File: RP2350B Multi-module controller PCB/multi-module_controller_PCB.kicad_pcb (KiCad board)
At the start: 4 copper layers, 59.8 x 85 mm, 71 parts, among them J4 SM03B-SRSS-TB, SW1 SW_Push, SW10 BTN_MDL, SW2 SW_Push, SW3 BTN_LEFT, SW4 BTN_UP, SW5 BTN_OK, SW6 BTN_DOWN, SW7 BTN_RIGHT, SW8 BTN_BACK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

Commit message: all core components placed and routed
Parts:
- added J5: USB_C_Receptacle_USB2.0_14P, Connector_USB:USB_C_Receptacle_G-Switch_GT-USB-7010ASV, F.Cu at (100.1, 71.8)
- added J6: USB_C_Receptacle_USB2.0_14P, Connector_USB:USB_C_Receptacle_G-Switch_GT-USB-7010ASV, F.Cu at (62.9, 87.0)
- added J7: Module_Bay, Connector_PinHeader_2.54mm:PinHeader_1x08_P2.54mm_Vertical, F.Cu at (60.7, 135.7)
- added J8: USB_A, Connector_USB:USB_A_Connfly_DS1095, F.Cu at (72.0, 97.3)
- moved R20 74.1 mm to (64.8, 135.1), turned to 90 degrees
- moved R21 65.9 mm to (65.1, 127.9)
- moved C19 65.0 mm to (91.9, 109.1), turned to 90 degrees
- moved R22 61.9 mm to (65.0, 125.5)
- moved R5 60.2 mm to (93.3, 73.5), turned to 180 degrees
- moved R12 59.9 mm to (93.3, 72.3), turned to 180 degrees
- moved C24 58.7 mm to (65.4, 131.4), turned to -90 degrees
- moved C25 52.2 mm to (63.3, 131.7), turned to -90 degrees
- moved R17 49.9 mm to (79.0, 93.0), turned to 90 degrees
- moved R14 49.7 mm to (77.9, 93.0), turned to 90 degrees
- moved R19 46.2 mm to (79.2, 82.8), turned to -90 degrees
- moved R18 45.3 mm to (78.0, 82.8), turned to -90 degrees
- moved C23 37.6 mm to (93.5, 77.0), turned to 180 degrees
- moved R23 28.5 mm to (63.9, 80.2), turned to 180 degrees
- moved R24 27.7 mm to (63.9, 78.4), turned to 180 degrees
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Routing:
- net VBUS: track 12.1 -> 122.9 mm, vias 0 -> 4
- net GND: track 33.9 -> 126.7 mm, vias 28 -> 46
- net /GPIO13: track 8.02 -> 55.8 mm, vias 0 -> 2
- net /GPIO12: track 10.2 -> 52.5 mm, vias 0 -> 2
- net /GPIO24: track 6.66 -> 42.8 mm
- net /GPIO16: track 6.29 -> 40.3 mm, vias 0 -> 2
- net +3V3: track 52.9 -> 83.0 mm, vias 3 -> 18
- net /GPIO11: track 2.07 -> 31.1 mm, vias 0 -> 2
- net Net-(U6-OUTA): track 0.00 -> 27.3 mm, vias 0 -> 3
- net /GPIO10: track 1.97 -> 27.9 mm
- net /GPIO22: track 3.59 -> 26.3 mm, vias 0 -> 2
- net /GPIO9: track 1.86 -> 23.7 mm
- net /GPIO23: track 3.41 -> 23.2 mm, vias 0 -> 2
- net Net-(U5-HSD1+): track 0.00 -> 18.2 mm
- net /GPIO7: track 1.00 -> 19.2 mm, vias 0 -> 2
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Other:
- board size 59.8 x 85 mm -> 59.8 x 84.4 mm
- board text added: "2.5, 2.9"

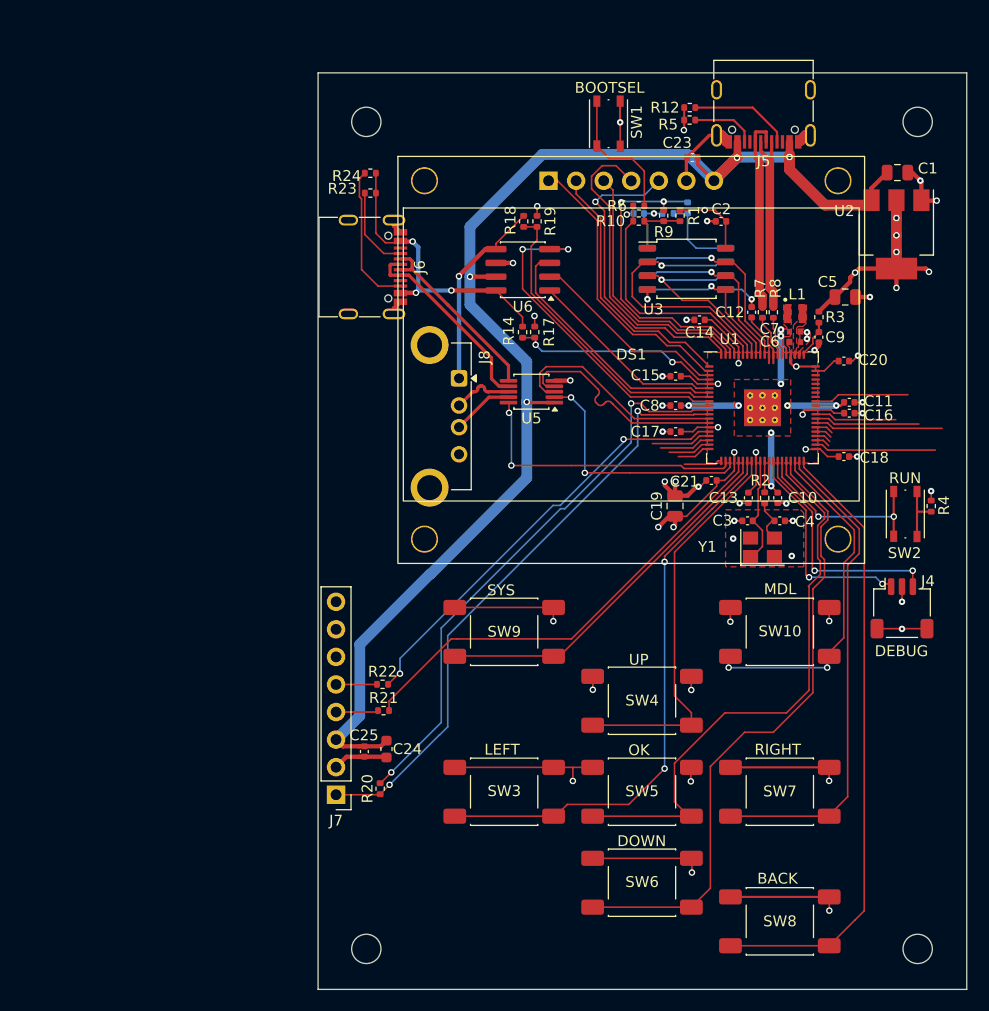
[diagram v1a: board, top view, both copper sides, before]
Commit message: minor tweaks to USB port overhang positioning
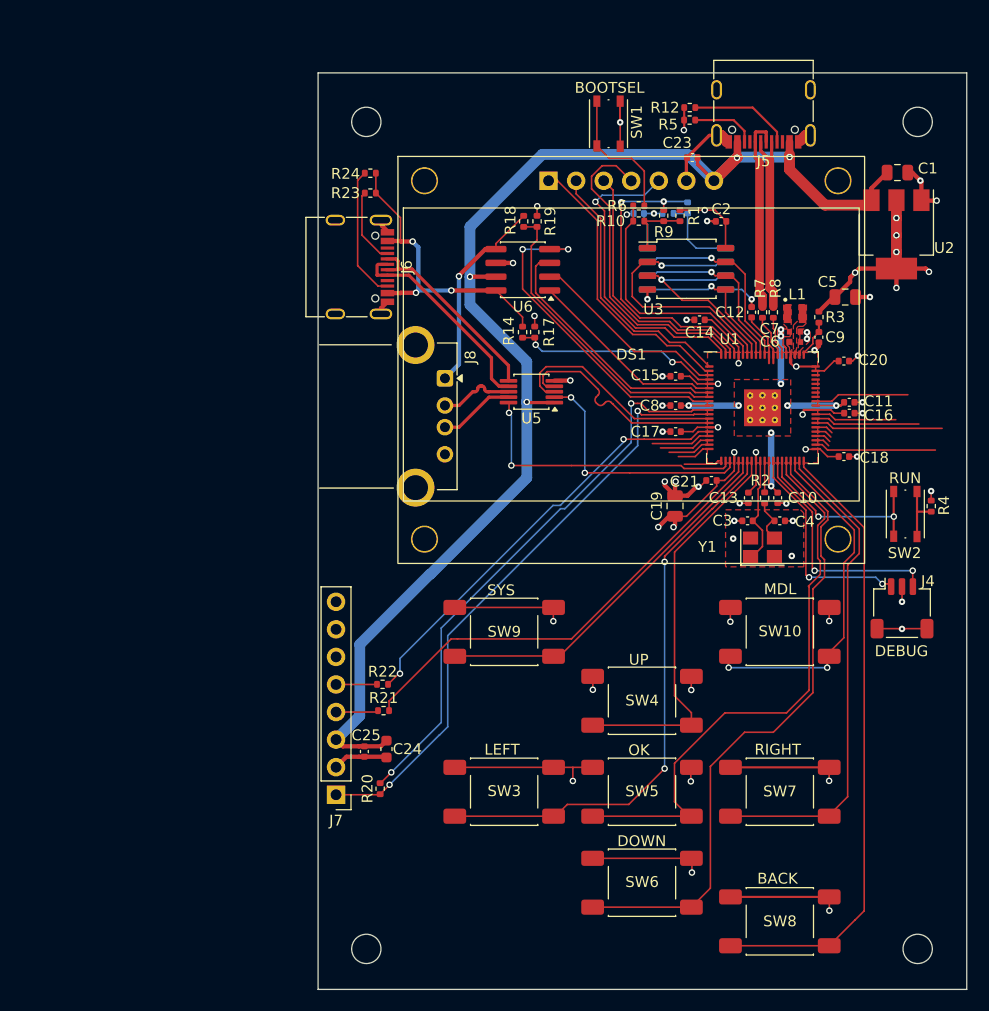
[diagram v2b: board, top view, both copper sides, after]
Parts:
- moved J8 1.30 mm to (70.7, 97.3)
- moved J6 1.20 mm to (61.7, 87.0)
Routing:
- net Net-(U6-OUTA): track 27.3 -> 28.7 mm
- net Net-(J8-D-): track 5.66 -> 6.96 mm
- net Net-(J8-D+): track 5.70 -> 7.00 mm
- net Net-(U5-HSD1-): track 17.0 -> 18.1 mm
- net Net-(U5-HSD1+): track 18.2 -> 19.3 mm
- net Net-(J6-CC2): track 13.4 -> 12.3 mm
- net Net-(J8-VBUS): track 17.6 -> 18.6 mm
- net Net-(J6-CC1): track 7.82 -> 7.03 mm
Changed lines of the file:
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@@
 		(tags "CMS SOT")
 		(property "Reference" "U2"
-			(at -2.15 4.8 0)
+			(at 1.25 -4.4 0)
 			(layer "F.SilkS")
 			(effects
@@
 	(footprint "Connector_USB:USB_A_Connfly_DS1095"
 		(layer "F.Cu")
-		(at 72.0428 97.2918 -90)
+		(at 70.7428 97.2918 -90)
 		(descr "USB type A receptacle, THT, horizontal, https://en.connfly.com/static/upload/file/DS1095.pdf")
 		(tags "Connfly female socket through-hole")
@@
 		(tags "capacitor")
 		(property "Reference" "C25"
-			(at -1.5 0.04 180)
+			(at -1.5 -0.16 180)
 			(layer "F.SilkS")
 			(effects
@@
 		(tags "resistor")
 		(property "Reference" "R24"
-			(at 2.1844 -0.2556 0)
+			(at 2.2844 -0.0556 0)
 			(layer "F.SilkS")
 			(effects
@@
 	(footprint "Connector_USB:USB_C_Receptacle_G-Switch_GT-USB-7010ASV"
 		(layer "F.Cu")
-		(at 62.9214 87.0366 -90)
+		(at 61.7214 87.0366 -90)
 		(descr "USB Type C, right-angle, SMT, https://datasheet.lcsc.com/lcsc/2204071530_G-Switch-GT-USB-7010ASV_C2988369.pdf")
 		(tags "USB C Type-C Receptacle SMD")
@@
 		(tags "resistor")
 		(property "Reference" "R23"
-			(at 2.5908 0.4048 0)
+			(at 2.2908 0.0048 0)
 			(layer "F.SilkS")
 			(effects
@@
 		)
 	)
+	(gr_line
+		(start 66 107.4)
+		(end 59.2 107.4)
+		(stroke
+			(width 0.12)
+			(type default)
+		)
+		(layer "F.SilkS")
+	)
+	(gr_line
+		(start 65.8 94.2)
+		(end 59.2 94.2)
+		(stroke
+			(width 0.12)
+			(type default)
+		)
+		(layer "F.SilkS")
+	)
 	(gr_rect
 		(start 59.055 69.145)
@@
 	)
 	(segment
-		(start 66.0464 91.3566)
-		(end 66.0464 90.8366)
+		(start 64.8464 91.3566)
+		(end 64.8464 90.8366)
 		(width 0.4)
 		(layer "F.Cu")
@@
 	)
 	(segment
-		(start 66.0464 83.2366)
-		(end 66.6464 83.8366)
+		(start 64.9464 83.2366)
+		(end 65.5464 83.8366)
 		(width 0.4)
 		(layer "F.Cu")
@@
 	)
 	(segment
-		(start 66.0464 90.8366)
-		(end 66.6464 90.2366)
+		(start 64.8464 90.8366)
+		(end 65.4464 90.2366)
 		(width 0.4)
 		(layer "F.Cu")
@@
 	)
 	(segment
-		(start 66.0464 82.7166)
-		(end 66.0464 83.2366)
+		(start 64.9464 82.7166)
+		(end 64.9464 83.2366)
 		(width 0.4)
 		(layer "F.Cu")
@@
 	)
 	(segment
-		(start 76.5983 97.524)
-		(end 76.5983 96.1055)
+		(start 66.4164 86.4846)
+		(end 66.2184 86.2866)
 		(width 0.3)
 		(layer "F.Cu")
@@
 	)
 	(segment
-		(start 76.5983 96.1055)
-		(end 71.0184 90.5256)
+		(start 66.4164 87.1728)
+		(end 66.4164 86.4846)
 		(width 0.3)
 		(layer "F.Cu")
@@
 	)
 	(segment
-		(start 67.7164 87.1728)
-		(end 67.6026 87.2866)
-		(width 0.3)
-		(layer "F.Cu")
-		(net 75)
-	)
-	(segment
-		(start 67.7164 87.2236)
-		(end 67.7164 87.1728)
+		(start 76.5983 96.1055)
+		(end 67.7164 87.2236)
 		(width 0.3)
 		(layer "F.Cu")
@@
 	)
 	(segment
-		(start 67.7164 87.1728)
-		(end 67.7164 86.4846)
+		(start 66.4672 87.2236)
+		(end 66.4164 87.1728)
 		(width 0.3)
 		(layer "F.Cu")
@@
 	)
 	(segment
-		(start 67.5184 86.2866)
-		(end 66.6464 86.2866)
+		(start 66.2184 86.2866)
+		(end 65.3464 86.2866)
 		(width 0.3)
 		(layer "F.Cu")
@@
 	)
 	(segment
-		(start 71.0184 90.5256)
-		(end 67.7164 87.2236)
+		(start 66.3026 87.2866)
+		(end 65.3464 87.2866)
 		(width 0.3)
 		(layer "F.Cu")
@@
 	)
 	(segment
-		(start 67.6026 87.2866)
-		(end 66.6464 87.2866)
+		(start 67.7164 87.2236)
+		(end 66.4672 87.2236)
 		(width 0.3)
 		(layer "F.Cu")
@@
 	)
 	(segment
-		(start 67.7164 86.4846)
-		(end 67.5184 86.2866)
+		(start 76.5983 97.524)
+		(end 76.5983 96.1055)
 		(width 0.3)
 		(layer "F.Cu")
@@
 	)
 	(segment
-		(start 74.8106 99.024)
-		(end 72.0428 101.7918)
+		(start 76.5983 99.024)
+		(end 74.8106 99.024)
 		(width 0.3)
 		(layer "F.Cu")
@@
 	)
 	(segment
-		(start 76.5983 99.024)
-		(end 74.8106 99.024)
+		(start 72.0428 101.7918)
+		(end 70.7428 101.7918)
 		(width 0.3)
 		(layer "F.Cu")
@@
 	)
 	(segment
-		(start 76.5983 98.024)
-		(end 75.733952 98.024)
+		(start 74.8106 99.024)
+		(end 72.0428 101.7918)
 		(width 0.3)
 		(layer "F.Cu")
-		(net 77)
+		(net 76)
 	)
 	(segment
-		(start 75.733952 98.024)
-		(end 75.0316 97.321648)
+		(start 67.4158 87.7866)
+		(end 65.4464 87.7866)
 		(width 0.3)
 		(layer "F.Cu")
@@
 	)
 	(segment
-		(start 65.6886 86.8724)
-		(end 65.7744 86.7866)
+		(start 64.5744 86.7866)
+		(end 65.4464 86.7866)
 		(width 0.3)
 		(layer "F.Cu")
@@
 	)
 	(segment
-		(start 65.7744 86.7866)
-		(end 66.6464 86.7866)
+		(start 65.4464 87.7866)
+		(end 64.4886 87.7866)
 		(width 0.3)
 		(layer "F.Cu")
@@
 	)
 	(segment
-		(start 66.6464 87.7866)
-		(end 65.6886 87.7866)
+		(start 75.733952 98.024)
+		(end 75.0316 97.321648)
 		(width 0.3)
 		(layer "F.Cu")
@@
 	)
 	(segment
-		(start 67.4158 87.7866)
-		(end 66.6464 87.7866)
+		(start 76.5983 98.024)
+		(end 75.733952 98.024)
 		(width 0.3)
 		(layer "F.Cu")
@@
 	)
 	(segment
-		(start 65.6886 87.7866)
-		(end 65.6886 86.8724)
+		(start 64.4886 87.7866)
+		(end 64.4886 86.8724)
 		(width 0.3)
 		(layer "F.Cu")
@@
 	)
 	(segment
+		(start 72.0428 99.7918)
+		(end 70.7428 99.7918)
+		(width 0.3)
+		(layer "F.Cu")
+		(net 78)
+	)
+	(segment
 		(start 73.75661 98.268)
 		(end 73.75661 98.25)
@@
 	)
 	(segment
-		(start 72.0428 87.8924)
-		(end 72.0344 87.884)
+		(start 72.0344 96.0002)
+		(end 70.7428 97.2918)
 		(width 0.4)
 		(layer "B.Cu")
@@
 	)
 	(segment
-		(start 72.0428 96.8918)
-		(end 72.0428 87.8924)
+		(start 72.0344 87.884)
+		(end 72.0344 96.0002)
+		(width 0.4)
+		(layer "B.Cu")
+		(net 79)
+	)
+	(segment
+		(start 72.0428 87.8924)
+		(end 72.0344 87.884)
 		(width 0.4)
 		(layer "B.Cu")
@@
 	(segment
 		(start 66.6464 84.6366)
-		(end 66.4854 84.7976)
-		(width 0.15)
+		(end 65.4464 84.6366)
+		(width 0.4)
 		(layer "F.Cu")
 		(net 80)
 	)
 	(segment
-		(start 77.8968 92.525)
-		(end 77.8968 91.6488)
-		(width 0.15)
+		(start 66.6934 84.6836)
+		(end 66.6464 84.6366)
+		(width 0.4)
 		(layer "F.Cu")
 		(net 80)
 	)
 	(segment
-		(start 66.4854 84.7976)
-		(end 65.256747 84.7976)
+		(start 66.675 89.408)
+		(end 66.6464 89.4366)
+		(width 0.4)
+		(layer "F.Cu")
+		(net 80)
+	)
+	(segment
+		(start 77.8968 92.525)
+		(end 77.8968 91.6488)
 		(width 0.15)
 		(layer "F.Cu")
@@
 	)
 	(segment
-		(start 66.6934 84.6836)
-		(end 66.6464 84.6366)
-		(width 0.4)
-		(layer "F.Cu")
-		(net 80)
-	)
-	(segment
-		(start 64.3816 83.922453)
-		(end 64.3816 80.2222)
+		(start 64.3816 80.2222)
+		(end 64.3816 80.1184)
 		(width 0.15)
 		(layer "F.Cu")
@@
 	)
 	(segment
-		(start 64.3816 80.2222)
-		(end 64.3816 80.1184)
+		(start 66.6464 82.487)
+		(end 66.6464 84.6366)
 		(width 0.15)
 		(layer "F.Cu")
@@
 	)
 	(segment
-		(start 66.675 89.408)
-		(end 66.6464 89.4366)
+		(start 66.6464 89.4366)
+		(end 65.4464 89.4366)
 		(width 0.4)
 		(layer "F.Cu")
@@
 	)
 	(segment
-		(start 65.256747 84.7976)
-		(end 64.3816 83.922453)
+		(start 64.38 80.1168)
+		(end 64.38 78.3878)
 		(width 0.15)
 		(layer "F.Cu")
@@
 	)
 	(segment
-		(start 64.38 80.1168)
-		(end 64.38 78.3878)
+		(start 64.3816 80.2222)
+		(end 66.6464 82.487)
 		(width 0.15)
 		(layer "F.Cu")
@@
 	)
 	(segment
-		(start 66.6464 85.7866)
-		(end 65.111 85.7866)
+		(start 63.1 84.1)
+		(end 64.7866 85.7866)
 		(width 0.15)
 		(layer "F.Cu")
@@
 	)
 	(segment
-		(start 65.111 85.7866)
-		(end 63.3616 84.0372)
+		(start 63.1 80.4838)
+		(end 63.1 84.1)
 		(width 0.15)
 		(layer "F.Cu")
@@
 	)
 	(segment
-		(start 63.3616 84.0372)
-		(end 63.3616 80.2222)
+		(start 64.7866 85.7866)
+		(end 65.4464 85.7866)
 		(width 0.15)
 		(layer "F.Cu")
@@
 	)
 	(segment
-		(start 63.0606 80.755474)
-		(end 63.0606 87.2686)
+		(start 63.3616 80.2222)
+		(end 63.1 80.4838)
 		(width 0.15)
 		(layer "F.Cu")
-		(net 86)
+		(net 85)
 	)
 	(segment
-		(start 64.5786 88.7866)
-		(end 66.6464 88.7866)
+		(start 62.7 79.0478)
+		(end 63.36 78.3878)
 		(width 0.15)
 		(layer "F.Cu")
@@
 	)
 	(segment
-		(start 63.36 78.3878)
-		(end 62.8656 78.8822)
+		(start 64.5786 88.7866)
+		(end 62.7 86.908)
 		(width 0.15)
 		(layer "F.Cu")
@@
 	)
 	(segment
-		(start 62.8656 80.560474)
-		(end 63.0606 80.755474)
+		(start 62.7 86.908)
+		(end 62.7 79.0478)
 		(width 0.15)
 		(layer "F.Cu")
@@
 	)
 	(segment
-		(start 63.0606 87.2686)
+		(start 65.4464 88.7866)
 		(end 64.5786 88.7866)
 		(width 0.15)
 		(layer "F.Cu")
-		(net 86)
-	)
-	(segment
-		(start 62.8656 78.8822)
-		(end 62.8656 80.560474)
-		(width 0.15)
-		(layer "F.Cu")

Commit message: completed layout, include production files, before adjusting component mounting
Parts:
- added J1: Conn_02x06_Odd_Even, Connector_PinSocket_2.54mm:PinSocket_2x06_P2.54mm_Vertical, F.Cu at (68.8, 71.6)
- added J9: ADC_Breakout, Connector_JST:JST_PH_B12B-PH-K_1x12_P2.00mm_Vertical, F.Cu at (116.3, 91.2)
- added R15: 10k, Resistor_SMD:R_0402_1005Metric, F.Cu at (83.3, 86.5)
- added R16: 10k, Resistor_SMD:R_0402_1005Metric, F.Cu at (83.2, 88.1)
- C24: footprint Capacitor_SMD:C_0603_1608Metric -> Capacitor_SMD:C_0805_2012Metric
- J4: footprint Connector_JST:JST_SH_SM03B-SRSS-TB_1x03-1MP_P1.00mm_Horizontal -> Connector_PinHeader_2.54mm:PinHeader_1x03_P2.54mm_Vertical
- moved R4 25.9 mm to (115.2, 135.0), turned to -90 degrees
- moved SW2 21.4 mm to (114.0, 131.2)
- moved J4 3.24 mm to (111.1, 121.2), turned to 90 degrees
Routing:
- net VBUS: track 122.9 -> 155.2 mm, vias 4 -> 5
- net GND: track 126.7 -> 148.0 mm, vias 46 -> 47
- net /RUN: track 17.6 -> 36.7 mm
- net /GPIO42_ADC2: track 0.00 -> 18.3 mm
- net /GPIO43_ADC3: track 0.00 -> 17.2 mm
- net /GPIO44_ADC4: track 0.00 -> 15.0 mm
- net /GPIO45_ADC5: track 0.00 -> 13.8 mm
- net /GPIO46_ADC6: track 0.00 -> 13.1 mm
- net /GPIO47_ADC7: track 0.00 -> 12.3 mm
- net /GPIO41_ADC1: track 8.75 -> 20.7 mm
- net +3V3: track 83.0 -> 94.8 mm, vias 18 -> 19
- net /GPIO40_ADC0: track 7.60 -> 18.1 mm
- net /GPIO38: track 11.9 -> 1.81 mm
- net /GPIO33: track 11.2 -> 1.31 mm
- net /GPIO39: track 9.72 -> 1.91 mm
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- added copper zone on B.Cu, net +1V1
- added copper zone on In2.Cu, net +3V3
- added copper zone on In1.Cu, net GND
- removed copper zone on In1.Cu, net +3V3
- removed copper zone on In2.Cu, net GND
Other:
- board text added: "3V3"
- board text added: "5V"
- board text added: "ADC0"
- board text added: "ADC1"
- board text added: "ADC2"
- board text added: "ADC3"
- board text added: "ADC4"
- board text added: "ADC5"
- board text added: "ADC6"
- board text added: "ADC7"
- board text added: "GND"
- board text added: "SWC"
- board text added: "SWD"
- board text added: "VBUS"
